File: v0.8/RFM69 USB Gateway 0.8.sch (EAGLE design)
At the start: 25 parts, among them CN1 MINIB, IC3 MCP1703CB, U2 ATMEGA328P-MU, X1 16 MHz

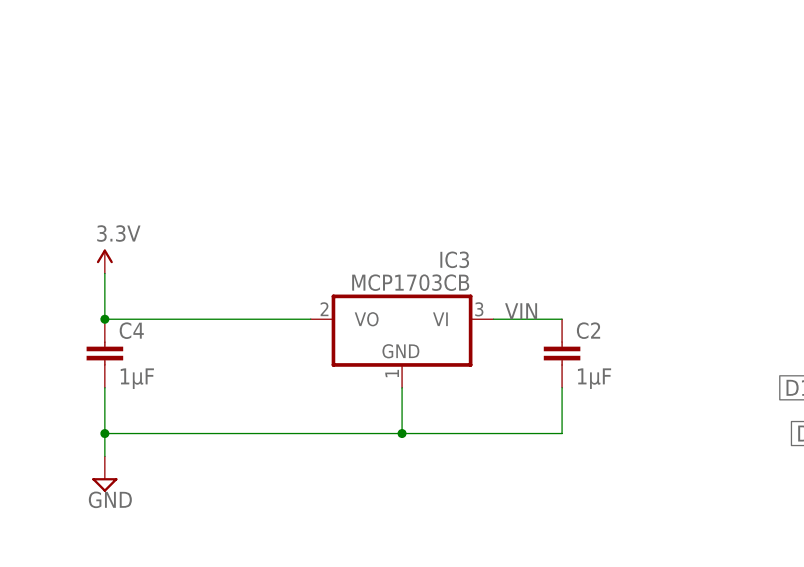
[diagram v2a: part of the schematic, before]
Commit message: Fixed silkscreen
Changed all fonts to vector; silkscreen now on layer 121, adjusted some
components and traces
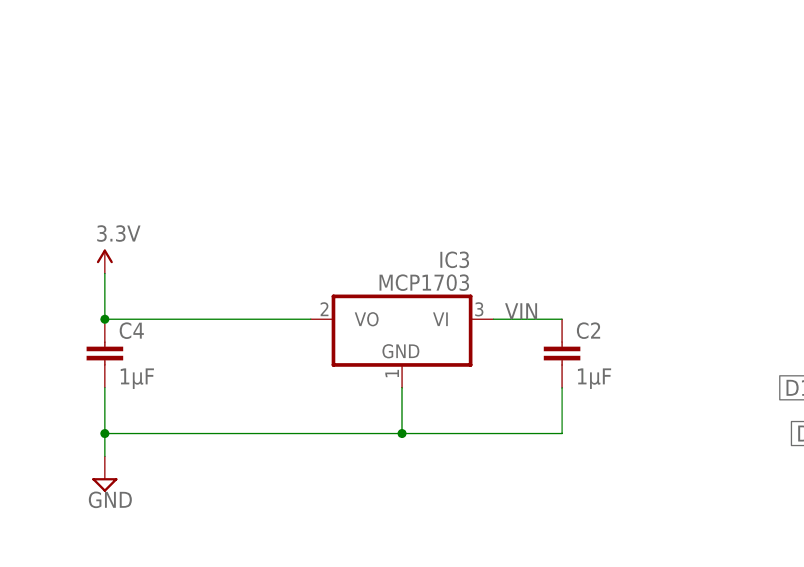
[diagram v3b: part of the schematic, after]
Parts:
- IC3: value MCP1703CB -> MCP1703
- U$2: value LED0805 -> Status
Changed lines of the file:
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@@
 <part name="X1" library="SparkFun" deviceset="RESONATOR" device="SMD" value="16 MHz"/>
 <part name="P+1" library="SparkFun" deviceset="VCC" device="" value="3.3V"/>
-<part name="IC3" library="linear" deviceset="MCP1703" device="CB"/>
+<part name="IC3" library="linear" deviceset="MCP1703" device="CB" value="MCP1703"/>
 <part name="C5" library="SparkFun" deviceset="CAP" device="0805" value="0.1μF"/>
 <part name="R1" library="LowPowerLab" deviceset="RESISTOR" device="0805" value="10KΩ"/>
 <part name="C4" library="LowPowerLab" deviceset="CAP" device="0805" value="1μF"/>
 <part name="C2" library="SparkFun" deviceset="CAP" device="0805" value="1μF"/>
-<part name="U$2" library="LowPowerLab" deviceset="LED" device="0805" value="LED0805"/>
+<part name="U$2" library="LowPowerLab" deviceset="LED" device="0805" value="Status"/>
 <part name="SUPPLY6" library="supply2" deviceset="GND" device=""/>
 <part name="R2" library="SparkFun" deviceset="RESISTOR" device="0805-RES" value="1KΩ"/>

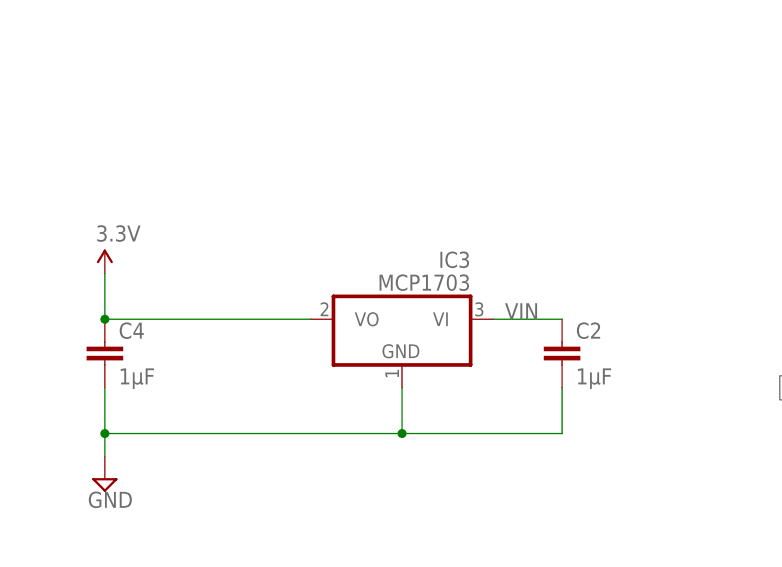
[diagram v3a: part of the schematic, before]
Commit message: Adjusted silkscreen
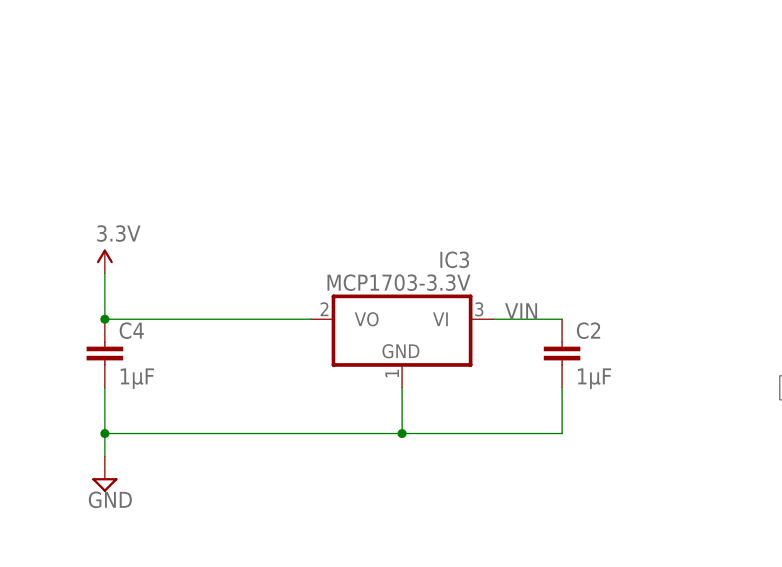
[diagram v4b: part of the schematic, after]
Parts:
- IC3: value MCP1703 -> MCP1703-3.3V
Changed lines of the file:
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@@
 <part name="X1" library="SparkFun" deviceset="RESONATOR" device="SMD" value="16 MHz"/>
 <part name="P+1" library="SparkFun" deviceset="VCC" device="" value="3.3V"/>
-<part name="IC3" library="linear" deviceset="MCP1703" device="CB" value="MCP1703"/>
+<part name="IC3" library="linear" deviceset="MCP1703" device="CB" value="MCP1703-3.3V"/>
 <part name="C5" library="SparkFun" deviceset="CAP" device="0805" value="0.1μF"/>
 <part name="R1" library="LowPowerLab" deviceset="RESISTOR" device="0805" value="10KΩ"/>
